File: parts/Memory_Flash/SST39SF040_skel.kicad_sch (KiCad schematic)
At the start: 39 parts, among them U1 BUF, U10 BUF, U11 BUF, U12 BUF, U13 BUF, U14 BUF, U15 BUF, U16 BUF, U17 BUF, U18 BUF, U19 BUF, U2 BUF, U20 INV, U21 INV, U22 BUF_G, U23 BUF_G, U24 BUF_G, U25 BUF_G, U26 BUF_G, U27 BUF_G, U28 BUF_G, U29 BUF_G, U3 BUF, U30 NOR3, U31 NOR3, U32 BUF_G, U33 BUF_G, U34 BUF_G, U35 BUF_G, U36 BUF_G, U37 BUF_G, U38 BUF_G, U39 BUF_G, U4 BUF, U5 BUF, U6 BUF, U7 BUF, U8 BUF, U9 BUF

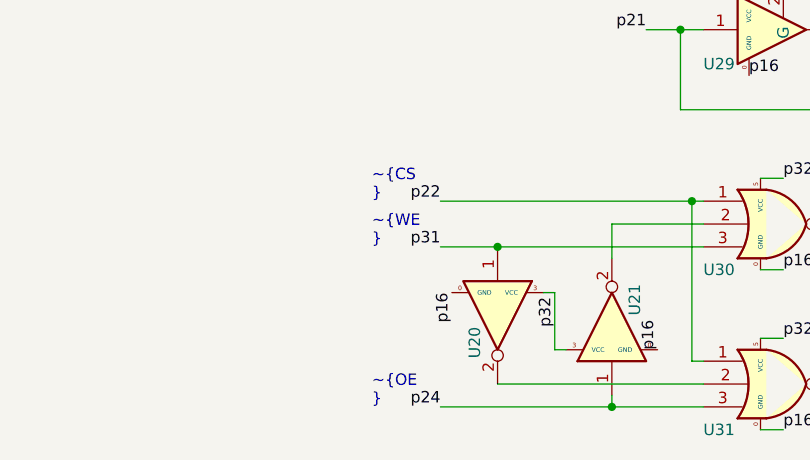
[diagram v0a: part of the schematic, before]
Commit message: Fixed small bug in schematic file (string format).
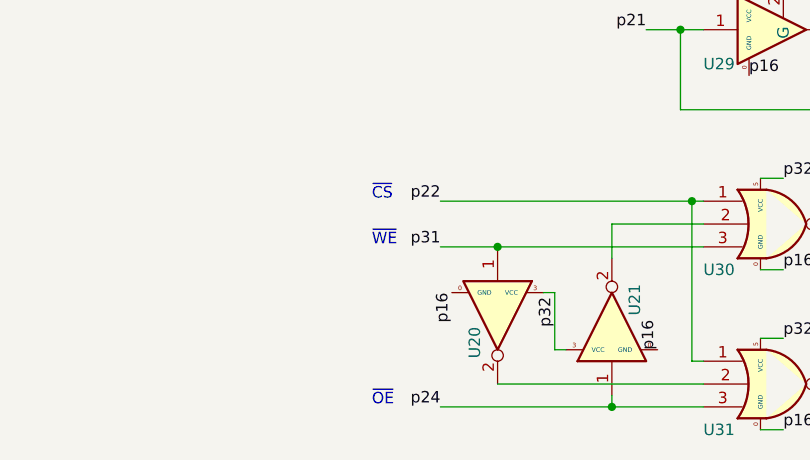
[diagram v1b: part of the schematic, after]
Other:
- note added: "~{CS}"
- note added: "~{OE}"
- note added: "~{WE}"
- note removed: "~{CS }"
- note removed: "~{OE }"
- note removed: "~{WE }"
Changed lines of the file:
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@@
 		)
 	)
-	(text "~{OE\n}"
+	(text "~{OE}"
 		(exclude_from_sim no)
 		(at 105.41 189.23 0)
@@
 		)
 	)
-	(text "~{CS\n}"
+	(text "~{CS}"
 		(exclude_from_sim no)
 		(at 105.41 166.37 0)
@@
 		)
 	)
-	(text "~{WE\n}"
+	(text "~{WE}"
 		(exclude_from_sim no)
 		(at 105.41 171.45 0)
